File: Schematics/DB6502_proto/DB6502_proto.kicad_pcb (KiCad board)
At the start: 2 copper layers, 133.3 x 105.4 mm, 55 parts, among them J1 System Bus, J10 AVR-ISP-6, J2 Controls, J3 Debug UART, J4 I/O Bus, J5 USB_B, SW1 Reset, U1 DS1813, U2 65C02S, U3 62256, U4 ATmega644PA-PU, U5 62256, U6 74AC138, U7 28C256, U8 22V10C, U9 FT230XS, Y1 20MHz

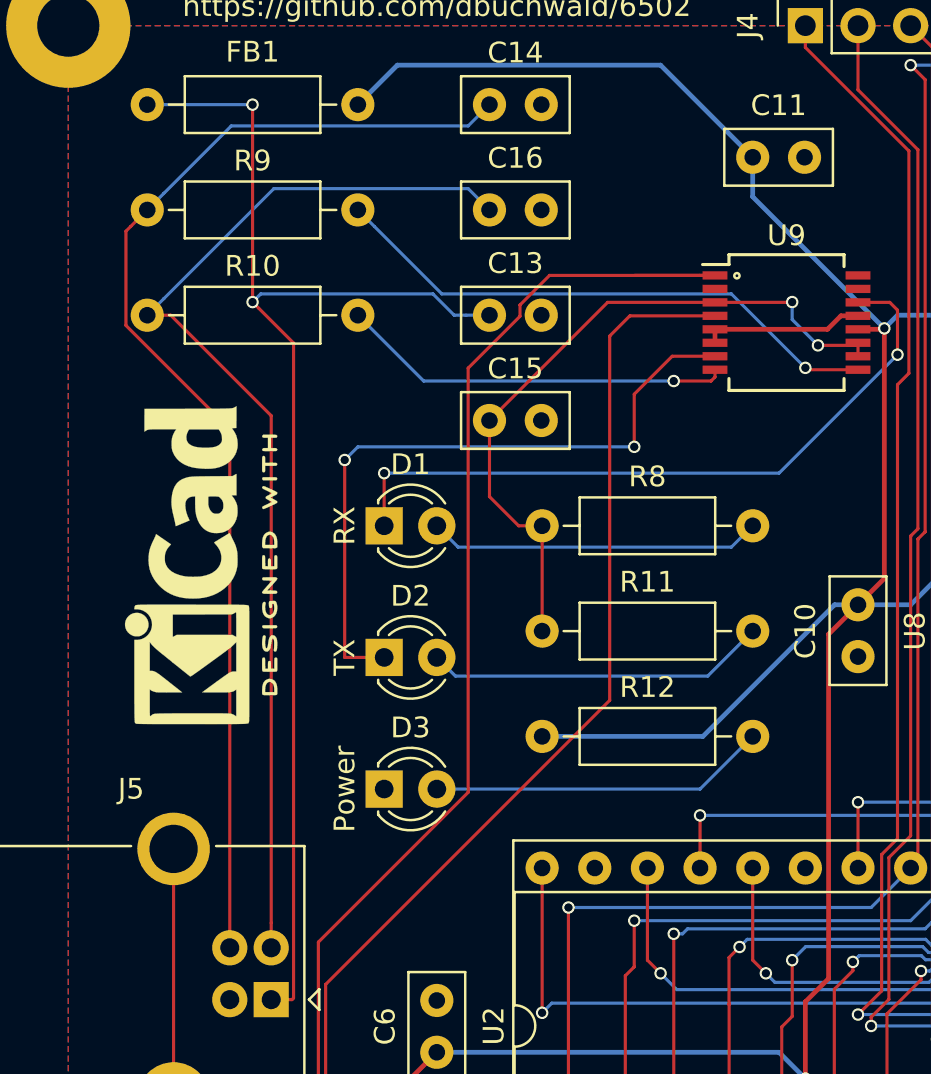
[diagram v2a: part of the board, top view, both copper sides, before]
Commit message: Fixed bug with D+/D- switched
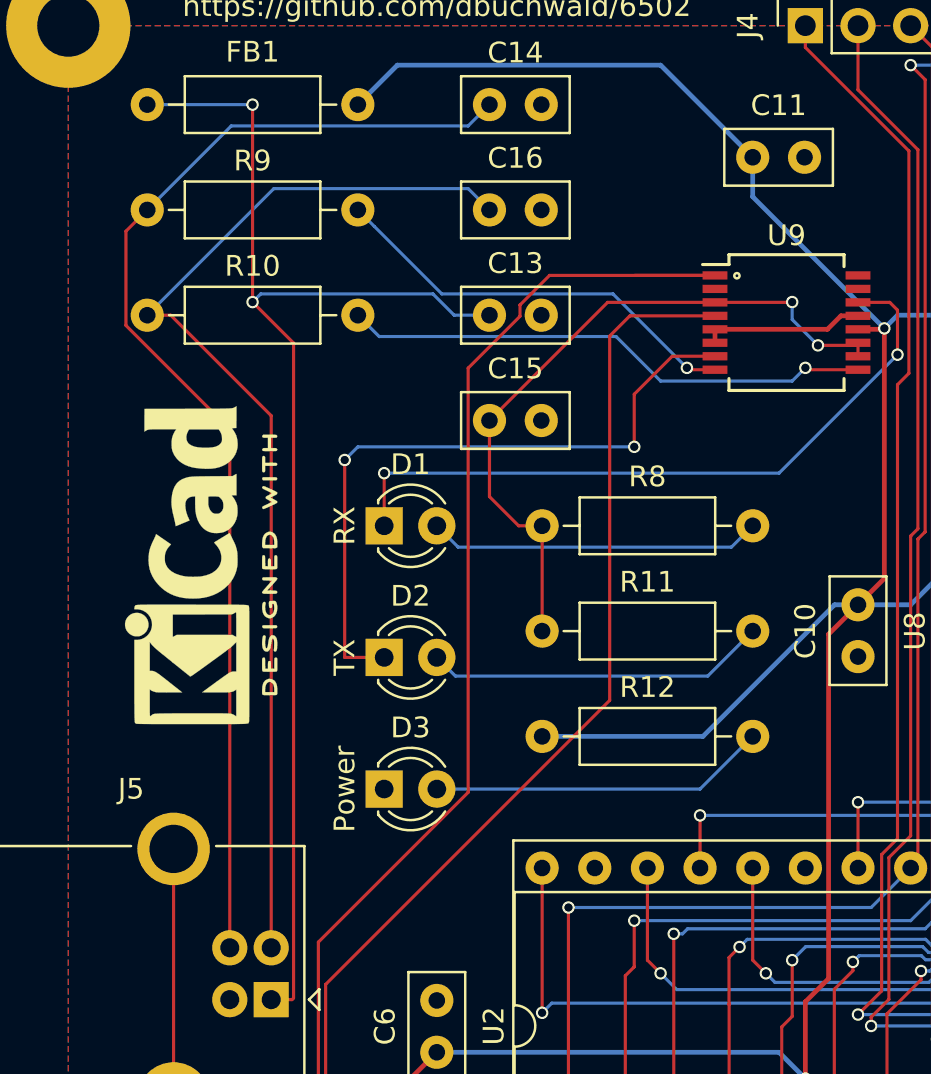
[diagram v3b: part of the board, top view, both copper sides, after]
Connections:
- R10 pad 2: USBD+ -> USBD-
- R9 pad 2: USBD- -> USBD+
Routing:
- net USBD-: track 27.3 -> 25.7 mm
- net USBD+: track 19.0 -> 20.4 mm
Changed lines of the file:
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@@
     (thickness 1.6)
     (drawings 137)
-    (tracks 1700)
+    (tracks 1695)
     (zones 0)
     (modules 55)
@@
     (fp_line (start 1.93 -1.25) (end 1.93 1.25) (layer F.Fab) (width 0.1))
     (pad 2 thru_hole oval (at 10.16 0) (size 1.6 1.6) (drill 0.8) (layers *.Cu *.Mask)
-      (net 79 USBD+))
+      (net 78 USBD-))
     (pad 1 thru_hole circle (at 0 0) (size 1.6 1.6) (drill 0.8) (layers *.Cu *.Mask)
       (net 9 "Net-(C16-Pad1)"))
@@
     (fp_line (start 1.93 -1.25) (end 1.93 1.25) (layer F.Fab) (width 0.1))
     (pad 2 thru_hole oval (at 10.16 0) (size 1.6 1.6) (drill 0.8) (layers *.Cu *.Mask)
-      (net 78 USBD-))
+      (net 79 USBD+))
     (pad 1 thru_hole circle (at 0 0) (size 1.6 1.6) (drill 0.8) (layers *.Cu *.Mask)
       (net 7 "Net-(C14-Pad1)"))
@@
   (segment (start 80.14863 45.72) (end 73.79863 52.07) (width 0.2286) (layer B.Cu) (net 5))
   (segment (start 81.28 45.72) (end 80.14863 45.72) (width 0.2286) (layer B.Cu) (net 5) (status 10))
-  (segment (start 58.42 69.85) (end 60.96 67.31) (width 0.2286) (layer F.Cu) (net 5))
-  (segment (start 58.42 74.295) (end 58.42 69.85) (width 0.2286) (layer F.Cu) (net 5))
+  (segment (start 58.42 69.85) (end 60.96 67.31) (width 0.2286) (layer F.Cu) (net 5) (status 20))
+  (segment (start 58.42 74.295) (end 58.42 69.85) (width 0.2286) (layer F.Cu) (net 5) (status 10))
   (via (at 52.07 21.59) (size 0.6) (drill 0.4) (layers F.Cu B.Cu) (net 6))
-  (segment (start 46.99 21.59) (end 52.07 21.59) (width 0.1524) (layer B.Cu) (net 6))
+  (segment (start 46.99 21.59) (end 52.07 21.59) (width 0.1524) (layer B.Cu) (net 6) (status 10))
   (via (at 52.07 31.115) (size 0.6) (drill 0.4) (layers F.Cu B.Cu) (net 6))
   (segment (start 52.07 21.59) (end 52.07 31.115) (width 0.1524) (layer F.Cu) (net 6))
   (segment (start 60.770333 30.721399) (end 61.798934 31.75) (width 0.1524) (layer B.Cu) (net 6))
-  (segment (start 61.798934 31.75) (end 62.36863 31.75) (width 0.1524) (layer B.Cu) (net 6))
+  (segment (start 61.798934 31.75) (end 63.5 31.75) (width 0.1524) (layer B.Cu) (net 6) (status 20))
   (segment (start 52.07 31.115) (end 52.463601 30.721399) (width 0.1524) (layer B.Cu) (net 6))
-  (segment (start 62.36863 31.75) (end 63.5 31.75) (width 0.1524) (layer B.Cu) (net 6))
   (segment (start 52.463601 30.721399) (end 60.770333 30.721399) (width 0.1524) (layer B.Cu) (net 6))
-  (segment (start 52.369999 31.414999) (end 52.07 31.115) (width 0.1524) (layer F.Cu) (net 6))
-  (segment (start 54.048601 33.093601) (end 52.369999 31.414999) (width 0.1524) (layer F.Cu) (net 6))
+  (segment (start 54.048601 33.093601) (end 52.07 31.115) (width 0.1524) (layer F.Cu) (net 6))
   (segment (start 54.048601 64.693799) (end 54.048601 33.093601) (width 0.1524) (layer F.Cu) (net 6))
   (segment (start 53.9724 64.77) (end 54.048601 64.693799) (width 0.1524) (layer F.Cu) (net 6))
-  (segment (start 52.97 64.77) (end 53.9724 64.77) (width 0.1524) (layer F.Cu) (net 6))
+  (segment (start 52.97 64.77) (end 53.9724 64.77) (width 0.1524) (layer F.Cu) (net 6) (status 10))
   (segment (start 62.471399 22.618601) (end 51.041399 22.618601) (width 0.1524) (layer B.Cu) (net 7))
-  (segment (start 47.789999 25.870001) (end 46.99 26.67) (width 0.1524) (layer B.Cu) (net 7))
-  (segment (start 51.041399 22.618601) (end 47.789999 25.870001) (width 0.1524) (layer B.Cu) (net 7))
-  (segment (start 63.5 21.59) (end 62.471399 22.618601) (width 0.1524) (layer B.Cu) (net 7))
-  (segment (start 46.190001 27.469999) (end 46.99 26.67) (width 0.1524) (layer F.Cu) (net 7))
-  (segment (start 45.961399 27.698601) (end 46.190001 27.469999) (width 0.1524) (layer F.Cu) (net 7))
+  (segment (start 51.041399 22.618601) (end 46.99 26.67) (width 0.1524) (layer B.Cu) (net 7) (status 20))
+  (segment (start 63.5 21.59) (end 62.471399 22.618601) (width 0.1524) (layer B.Cu) (net 7) (status 10))
+  (segment (start 45.961399 27.698601) (end 46.99 26.67) (width 0.1524) (layer F.Cu) (net 7) (status 20))
   (segment (start 45.961399 32.243729) (end 45.961399 27.698601) (width 0.1524) (layer F.Cu) (net 7))
   (segment (start 50.97 37.25233) (end 45.961399 32.243729) (width 0.1524) (layer F.Cu) (net 7))
-  (segment (start 50.97 62.27) (end 50.97 37.25233) (width 0.1524) (layer F.Cu) (net 7))
+  (segment (start 50.97 62.27) (end 50.97 37.25233) (width 0.1524) (layer F.Cu) (net 7) (status 10))
   (segment (start 74.38 31.13) (end 78.09 31.13) (width 0.1524) (layer F.Cu) (net 8) (status 10))
   (via (at 78.105 31.115) (size 0.6) (drill 0.4) (layers F.Cu B.Cu) (net 8))
@@
   (segment (start 66.04 41.91) (end 64.90863 41.91) (width 0.1524) (layer F.Cu) (net 8) (status 10))
   (segment (start 66.04 41.91) (end 66.04 46.99) (width 0.1524) (layer F.Cu) (net 8) (status 30))
-  (segment (start 47.789999 30.950001) (end 46.99 31.75) (width 0.1524) (layer B.Cu) (net 9))
-  (segment (start 53.098601 25.641399) (end 47.789999 30.950001) (width 0.1524) (layer B.Cu) (net 9))
+  (segment (start 53.098601 25.641399) (end 46.99 31.75) (width 0.1524) (layer B.Cu) (net 9) (status 20))
   (segment (start 62.471399 25.641399) (end 53.098601 25.641399) (width 0.1524) (layer B.Cu) (net 9))
-  (segment (start 63.5 26.67) (end 62.471399 25.641399) (width 0.1524) (layer B.Cu) (net 9))
-  (segment (start 52.97 36.59863) (end 52.97 61.067919) (width 0.1524) (layer F.Cu) (net 9))
-  (segment (start 52.97 61.067919) (end 52.97 62.27) (width 0.1524) (layer F.Cu) (net 9))
+  (segment (start 63.5 26.67) (end 62.471399 25.641399) (width 0.1524) (layer B.Cu) (net 9) (status 10))
+  (segment (start 52.97 36.59863) (end 52.97 62.27) (width 0.1524) (layer F.Cu) (net 9) (status 20))
   (segment (start 48.12137 31.75) (end 52.97 36.59863) (width 0.1524) (layer F.Cu) (net 9))
-  (segment (start 46.99 31.75) (end 48.12137 31.75) (width 0.1524) (layer F.Cu) (net 9))
+  (segment (start 46.99 31.75) (end 48.12137 31.75) (width 0.1524) (layer F.Cu) (net 9) (status 10))
   (segment (start 75.171399 42.938601) (end 76.2 41.91) (width 0.1524) (layer B.Cu) (net 10) (status 20))
   (segment (start 61.988601 42.938601) (end 75.171399 42.938601) (width 0.1524) (layer B.Cu) (net 10))
@@
   (segment (start 99.06 87.174002) (end 100.245001 88.359003) (width 0.1524) (layer F.Cu) (net 64))
   (segment (start 50.991399 82.741399) (end 50.991399 77.913601) (width 0.1524) (layer F.Cu) (net 64))
-  (segment (start 52.07 83.82) (end 50.991399 82.741399) (width 0.1524) (layer F.Cu) (net 64))
+  (segment (start 52.07 83.82) (end 50.991399 82.741399) (width 0.1524) (layer F.Cu) (net 64) (status 10))
   (segment (start 50.991399 77.913601) (end 55.245 73.66) (width 0.1524) (layer F.Cu) (net 64))
-  (segment (start 73.6276 29.83) (end 74.38 29.83) (width 0.1524) (layer F.Cu) (net 64))
-  (segment (start 66.39767 29.83) (end 73.6276 29.83) (width 0.1524) (layer F.Cu) (net 64))
+  (segment (start 66.39767 29.83) (end 74.38 29.83) (width 0.1524) (layer F.Cu) (net 64) (status 20))
   (segment (start 64.971399 31.256271) (end 66.39767 29.83) (width 0.1524) (layer F.Cu) (net 64))
   (segment (start 64.971399 31.800931) (end 64.971399 31.256271) (width 0.1524) (layer F.Cu) (net 64))
@@
   (segment (start 81.28 34.38) (end 78.83 34.38) (width 0.1524) (layer F.Cu) (net 78) (status 10))
   (segment (start 78.83 34.38) (end 78.74 34.29) (width 0.1524) (layer F.Cu) (net 78))
-  (segment (start 57.949999 27.469999) (end 57.15 26.67) (width 0.1524) (layer B.Cu) (net 78))
-  (segment (start 61.201399 30.721399) (end 57.949999 27.469999) (width 0.1524) (layer B.Cu) (net 78))
-  (segment (start 75.171399 30.721399) (end 61.201399 30.721399) (width 0.1524) (layer B.Cu) (net 78))
-  (segment (start 78.74 34.29) (end 75.171399 30.721399) (width 0.1524) (layer B.Cu) (net 78))
-  (segment (start 57.15 31.75) (end 60.325 34.925) (width 0.1524) (layer B.Cu) (net 79))
-  (via (at 72.39 34.925) (size 0.6) (drill 0.4) (layers F.Cu B.Cu) (net 79))
-  (segment (start 60.325 34.925) (end 72.39 34.925) (width 0.1524) (layer B.Cu) (net 79))
-  (segment (start 74.38 34.7324) (end 74.38 34.38) (width 0.1524) (layer F.Cu) (net 79))
-  (segment (start 74.1874 34.925) (end 74.38 34.7324) (width 0.1524) (layer F.Cu) (net 79))
-  (segment (start 72.39 34.925) (end 74.1874 34.925) (width 0.1524) (layer F.Cu) (net 79))
+  (segment (start 58.178601 32.778601) (end 69.608601 32.778601) (width 0.1524) (layer B.Cu) (net 78))
+  (segment (start 57.15 31.75) (end 58.178601 32.778601) (width 0.1524) (layer B.Cu) (net 78))
+  (segment (start 69.608601 32.778601) (end 71.755 34.925) (width 0.1524) (layer B.Cu) (net 78))
+  (segment (start 78.105 34.925) (end 78.74 34.29) (width 0.1524) (layer B.Cu) (net 78))
+  (segment (start 71.755 34.925) (end 78.105 34.925) (width 0.1524) (layer B.Cu) (net 78))
+  (via (at 73.025 34.29) (size 0.6) (drill 0.4) (layers F.Cu B.Cu) (net 79))
+  (segment (start 74.38 34.38) (end 73.115 34.38) (width 0.1524) (layer F.Cu) (net 79))
+  (segment (start 73.115 34.38) (end 73.025 34.29) (width 0.1524) (layer F.Cu) (net 79))
+  (segment (start 57.949999 27.469999) (end 57.15 26.67) (width 0.1524) (layer B.Cu) (net 79))
+  (segment (start 69.456399 30.721399) (end 61.201399 30.721399) (width 0.1524) (layer B.Cu) (net 79))
+  (segment (start 61.201399 30.721399) (end 57.949999 27.469999) (width 0.1524) (layer B.Cu) (net 79))
+  (segment (start 73.025 34.29) (end 69.456399 30.721399) (width 0.1524) (layer B.Cu) (net 79))
   (segment (start 73.66 54.61) (end 76.2 52.07) (width 0.1524) (layer B.Cu) (net 86) (status 20))
   (segment (start 60.96 54.61) (end 73.66 54.61) (width 0.1524) (layer B.Cu) (net 86) (status 10))

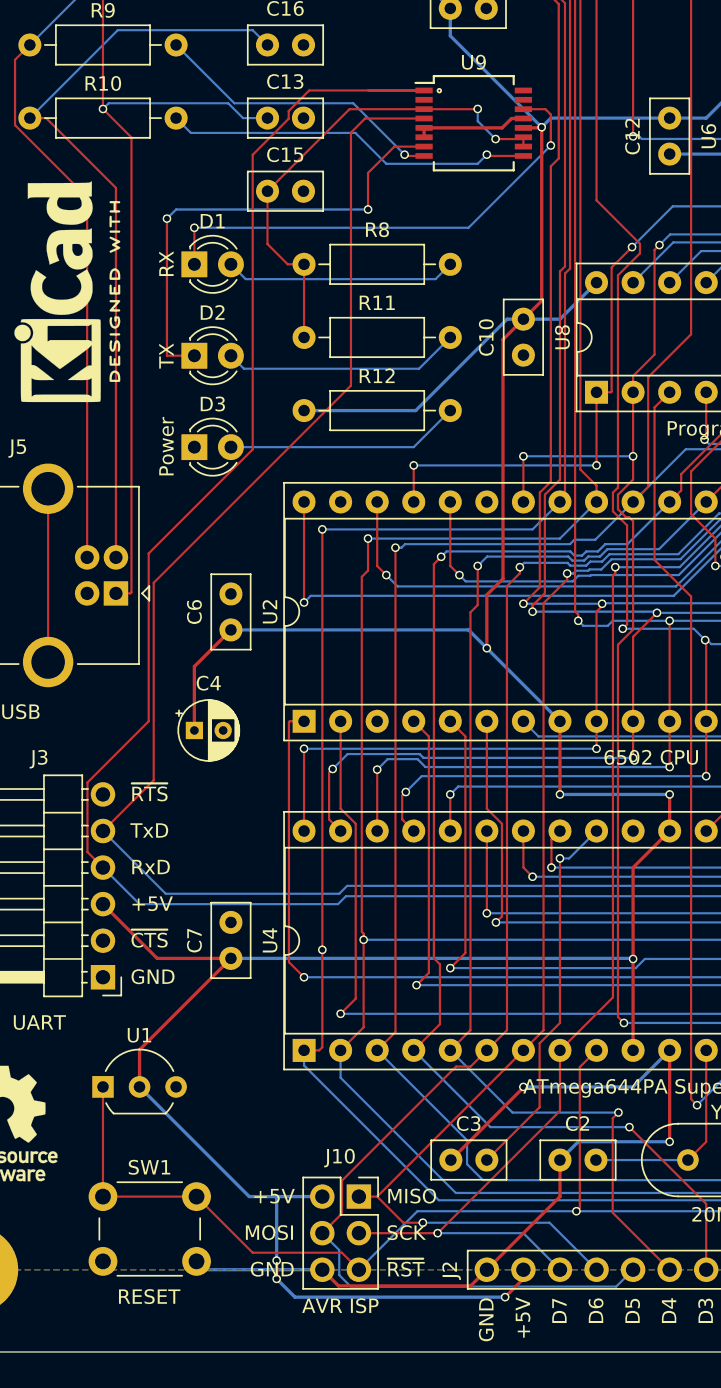
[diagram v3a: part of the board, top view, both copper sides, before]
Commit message: Fixed issue with AVR ISP port horizontal flip
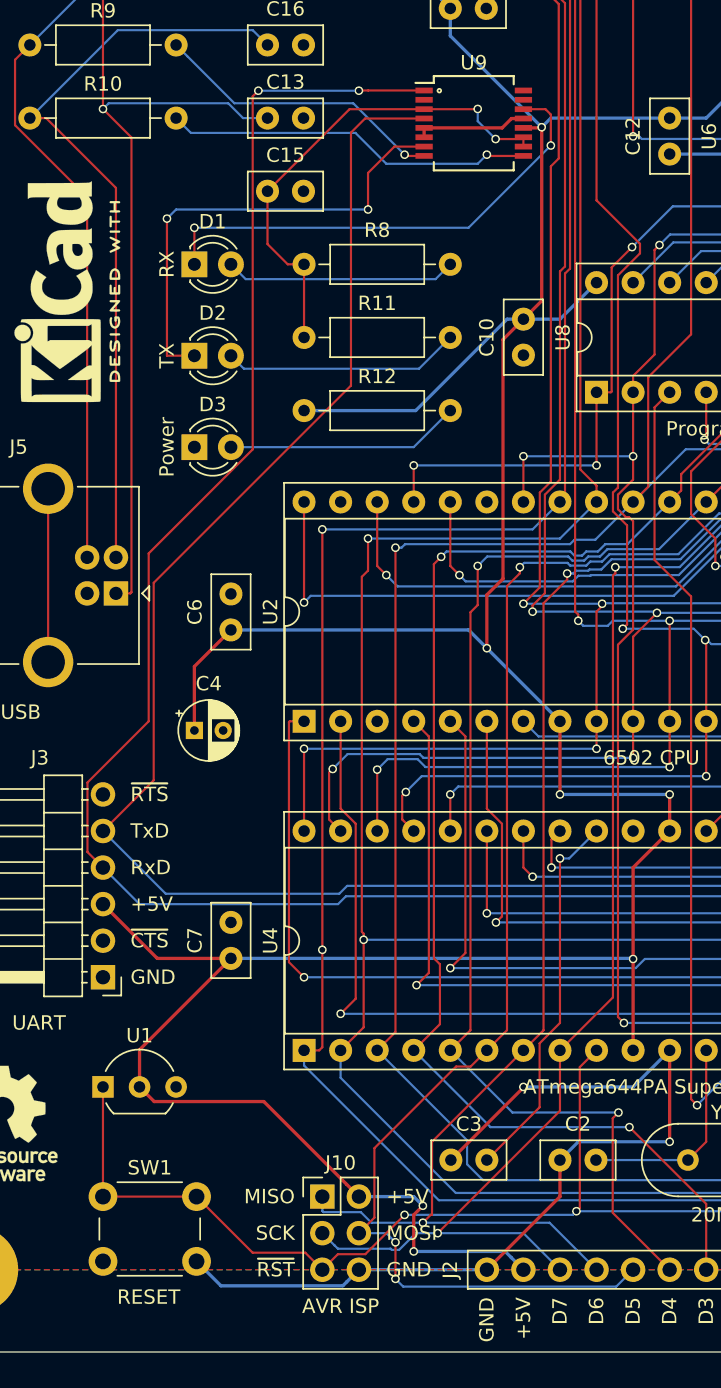
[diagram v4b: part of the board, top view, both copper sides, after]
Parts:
- J10: footprint Connector_PinSocket_2.54mm:PinSocket_2x03_P2.54mm_Vertical -> Connector_PinHeader_2.54mm:PinHeader_2x03_P2.54mm_Vertical
- moved J10 2.54 mm to (67.3, 106.7)
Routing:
- net +5V: track 475.5 -> 470.4 mm, vias 12 -> 11
- net d6: track 248.9 -> 252.5 mm
- net d7: track 239.2 -> 242.7 mm
- net d5: track 261.4 -> 258.3 mm, vias 1 -> 3
- net RxD_DBG: track 132.3 -> 130.5 mm, vias 1 -> 3
- net GND: track 240.7 -> 241.5 mm
- net ~RES: vias 1 -> 2
